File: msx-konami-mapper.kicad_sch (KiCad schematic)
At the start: 10 parts, among them SW1 Bonus Games, U1 SST39SF040, U3 74LS670, U4 74LS02

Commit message: Better explainer
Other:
- note added: "A14 = Page 0 (unpaged) A13+A14 = Page 1 A15 = Page 2 A13 + A15 = Page 3 Essentially, A13 or A15 = paged neither A13 nor A15 = unpaged"
- note removed: "A14 = Page 0 (unpaged) A13+A14 = Page 1 A15 = Page 2 A13 + A15 = Page 3 A15 doesn't seem to actually matter for the mirroring, so we probably want slot sel and read/write to a13, a14... do we need an additional '02 for decoding?"
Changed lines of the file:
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@@
 		)
 	)
-	(text "A14 = Page 0 (unpaged)\nA13+A14 = Page 1\nA15 = Page 2\nA13 + A15 = Page 3\n\nA15 doesn't seem to actually matter for the mirroring,\nso we probably want slot sel and read/write to a13, a14...\ndo we need an additional '02 for decoding?"
+	(text "A14 = Page 0 (unpaged)\nA13+A14 = Page 1\nA15 = Page 2\nA13 + A15 = Page 3\n\nEssentially, A13 or A15 = paged\nneither A13 nor A15 = unpaged"
 		(exclude_from_sim no)
 		(at 71.628 90.932 0)

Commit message: Prepare for BOM release
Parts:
- U2: now left out of the parts list
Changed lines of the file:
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@@
 		(unit 1)
 		(exclude_from_sim no)
-		(in_bom yes)
+		(in_bom no)
 		(on_board yes)
 		(dnp no)

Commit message: DK part numbers
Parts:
- C2, C3: DigiKey (none) -> 399-9776-ND
- RN1: DigiKey (none) -> 4609X-101-103LF-ND
- U1: DigiKey (none) -> SST39SF040-70-4C-PHE-ND
- U3: DigiKey (none) -> 296-34025-5-ND
- U4: DigiKey (none) -> 296-1627-5-ND
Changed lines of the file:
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@@
+			)
+		)
+		(property "DigiKey" "399-9776-ND"
+			(at 210.82 142.24 0)
+			(effects
+				(font
+					(size 1.27 1.27)
+				)
+				(hide yes)
 			)
 		)
@@
 			)
 		)
+		(property "DigiKey" "296-1627-5-ND"
+			(at 95.25 44.45 0)
+			(effects
+				(font
+					(size 1.27 1.27)
+				)
+				(hide yes)
+			)
+		)
 		(pin "7"
 		)
@@
 		)
 		(property "Description" "quad 2-input NOR gate"
+			(at 95.25 27.94 0)
+			(effects
+				(font
+					(size 1.27 1.27)
+				)
+				(hide yes)
+			)
+		)
+		(property "DigiKey" "296-1627-5-ND"
 			(at 95.25 27.94 0)
 			(effects
@@
 			)
 		)
+		(property "DigiKey" "296-1627-5-ND"
+			(at 154.94 175.26 0)
+			(effects
+				(font
+					(size 1.27 1.27)
+				)
+				(hide yes)
+			)
+		)
 		(pin "2"
 		)
@@
 			)
 		)
+		(property "DigiKey" "399-9776-ND"
+			(at 224.79 142.24 0)
+			(effects
+				(font
+					(size 1.27 1.27)
+				)
+				(hide yes)
+			)
+		)
 		(pin "1"
 		)
@@
 			)
 		)
+		(property "DigiKey" "296-34025-5-ND"
+			(at 191.77 41.91 0)
+			(effects
+				(font
+					(size 1.27 1.27)
+				)
+				(hide yes)
+			)
+		)
 		(pin "1"
 		)
@@
 			)
 		)
+		(property "DigiKey" "SST39SF040-70-4C-PHE-ND"
+			(at 264.16 69.85 0)
+			(effects
+				(font
+					(size 1.27 1.27)
+				)
+				(hide yes)
+			)
+		)
 		(pin "19"
 		)
@@
 		)
 		(property "Description" "8 resistor network, star topology, bussed resistors, small US symbol"
+			(at 223.52 44.45 0)
+			(effects
+				(font
+					(size 1.27 1.27)
+				)
+				(hide yes)
+			)
+		)
+		(property "DigiKey" "4609X-101-103LF-ND"
 			(at 223.52 44.45 0)
 			(effects
@@
 			)
 		)
+		(property "DigiKey" "296-1627-5-ND"
+			(at 138.43 177.8 0)
+			(effects
+				(font
+					(size 1.27 1.27)
+				)
+				(hide yes)
+			)
+		)
 		(pin "2"
 		)
@@
 			(at 111.76 27.94 0)
 			(effects
+				(font
+					(size 1.27 1.27)
+				)
+				(hide yes)
+			)
+		)
+		(property "DigiKey" "296-1627-5-ND"
+			(at 111.76 27.94 0)
+			(effects

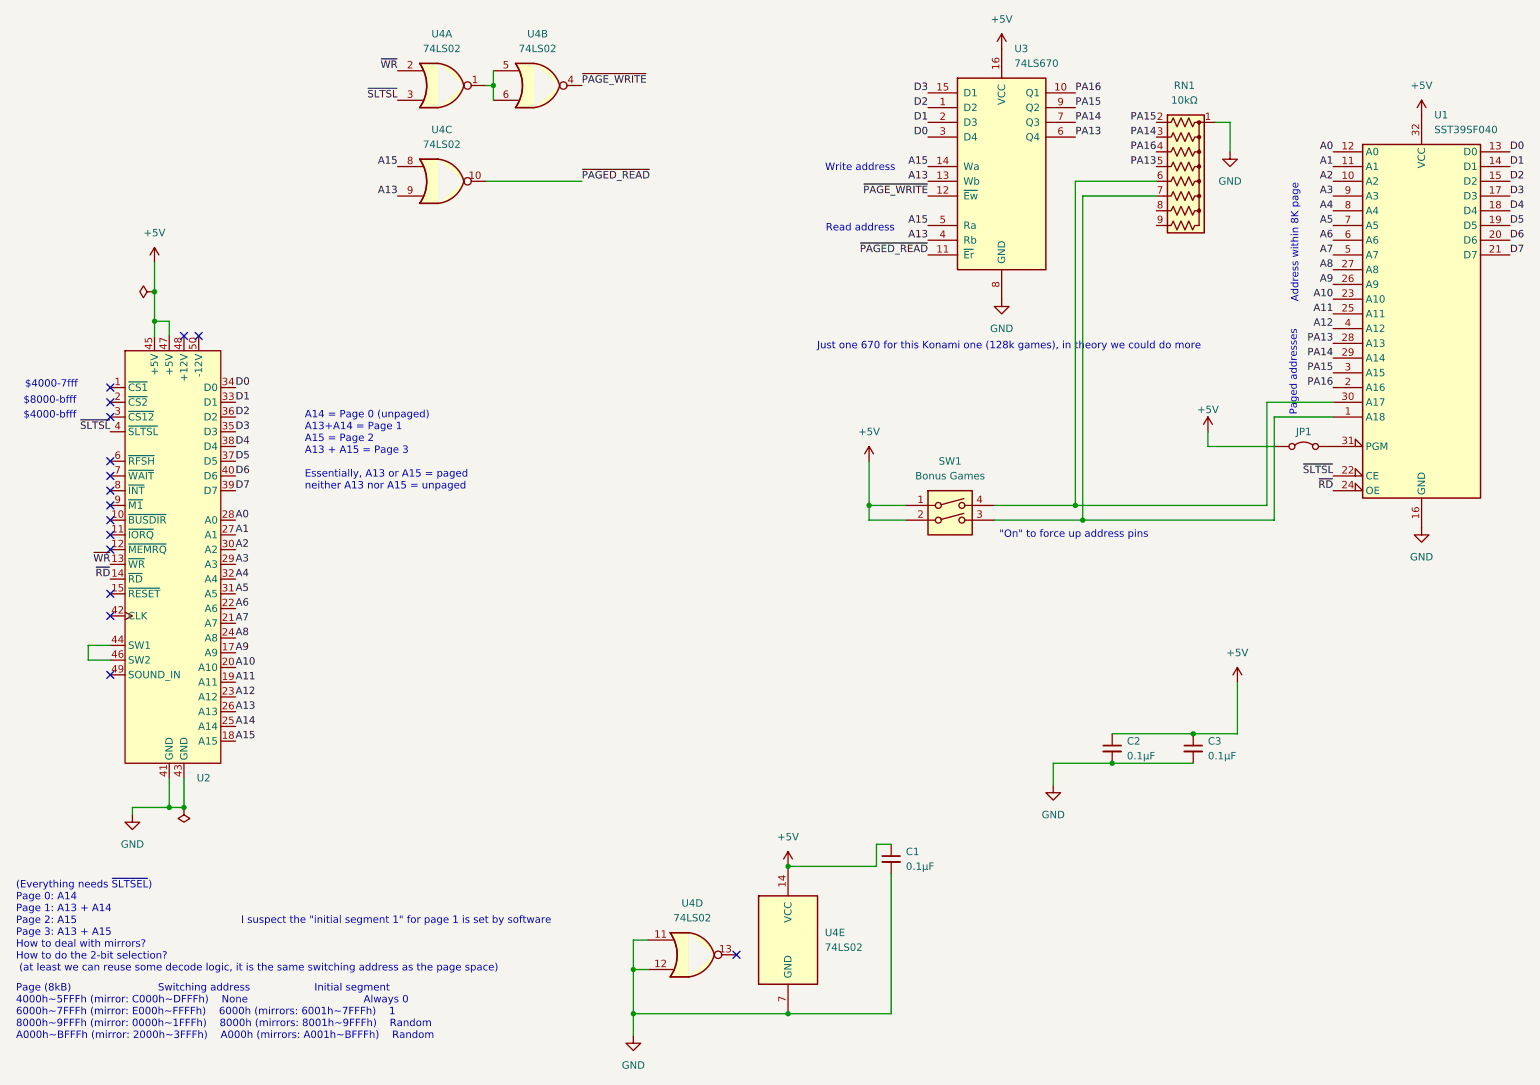
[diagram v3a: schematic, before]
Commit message: KiCad 9; add WR to ROM; fix +5V weak trace
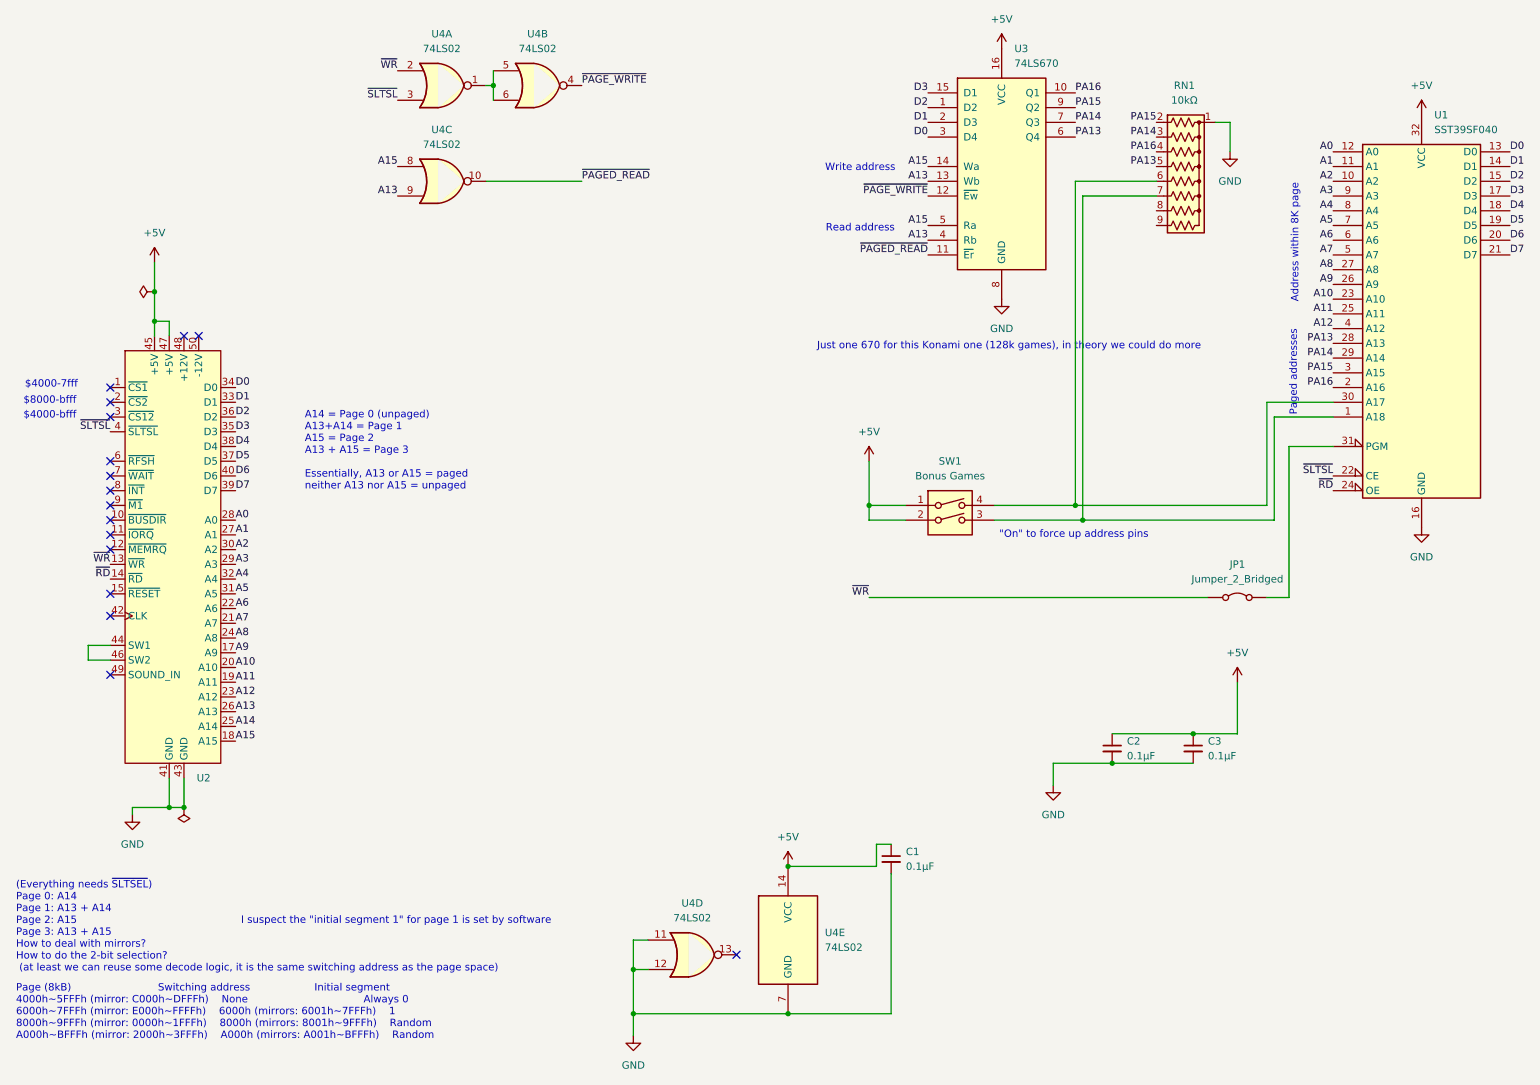
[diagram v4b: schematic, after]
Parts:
- JP1: footprint Jumper:SolderJumper-2_P1.3mm_Bridged_Pad1.0x1.5mm -> Jumper:SolderJumper-2_P1.3mm_Bridged_RoundedPad1.0x1.5mm
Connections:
- net +5V: no longer JP1.1 (A)
- net ~{WR}: now also JP1.1 (A)
